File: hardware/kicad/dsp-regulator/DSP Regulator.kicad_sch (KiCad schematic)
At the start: 73 parts, among them J1 Conn_01x15_Socket, J2 Conn_01x15_Socket, J3 1935161, J4 Wire con, J5 Wire con, Q16 BSS138, Q2 BSS138, Q3 BSS138, U2 LM2596S-ADJ, U3 LM2596S-ADJ, U4 LM2596S-ADJ, U8 TS5A3157-DCKR

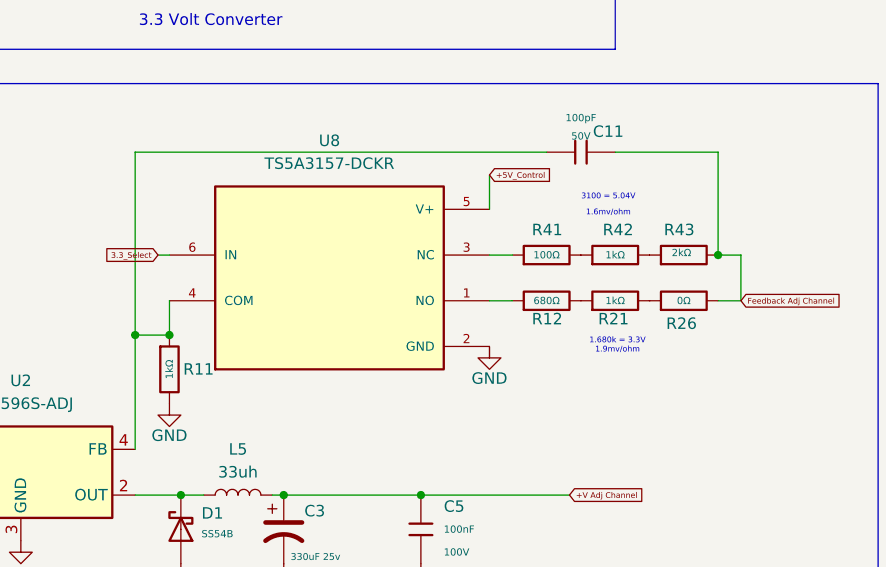
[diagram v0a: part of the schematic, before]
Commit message: hw(channel3): split J2 pin 06 to +V Adj Channel for CrowPanel 5V supply
- Split J2 pin 06 from +5V_Boot to dedicated +V Adj Channel net in
  both Rev-B schematics and netlists
- Reroute J21 pin 1 (CrowPanel display power) from +5V_Boot to
  +V Adj Channel in Rev-B HAT schematic and netlist
- PWR_FLAG at (123.19, 375.92) migrates to +V Adj Channel net via
  retained wire (374.65->375.92); J2 pins 08/10/12 remain on +5V_Boot
- DSP Regulator (PCB Rev-C prep): mark U8, R26, R43 as DNP;
  set R11=240 Ohm (lower FB->GND), R41=750 Ohm (future upper resistor)
- Update netlists manually to reflect schematic changes; re-export
  from KiCad GUI required for full ERC/DRC validation
- Connector contract: +V Adj Channel now PASS (was FAIL)

NOTE: R41 wire topology in DSP Regulator needs KiCad GUI edit to
connect as upper resistor (pin1->+V Adj Channel, pin2->FB).
VSENSE_ADJ+/-, ISET_MPU_Channel_3 failures are pre-existing.

Co-authored-by: Copilot <223556219+Copilot@users.noreply.github.com>
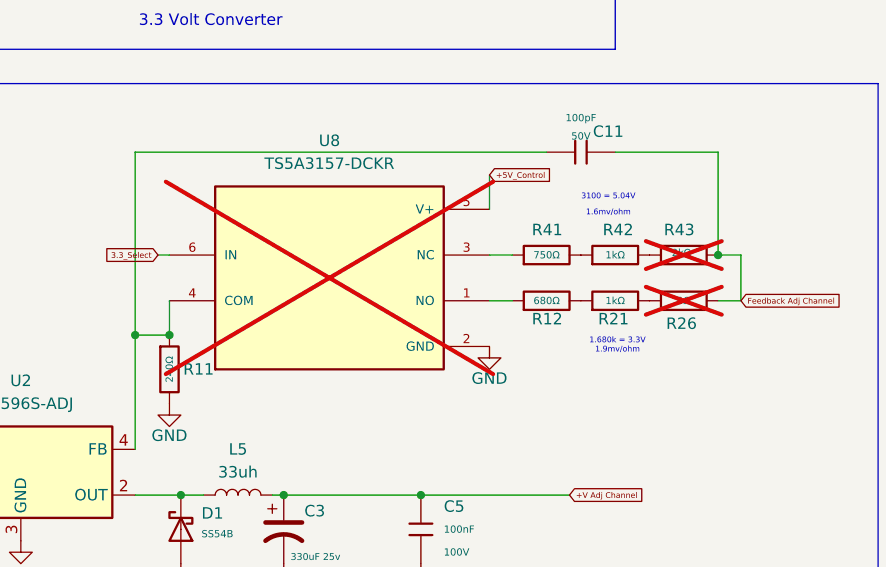
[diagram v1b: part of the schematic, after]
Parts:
- R11: value 1kΩ -> 240Ω
- R26, R43, U8: now not fitted
- R41: value 100Ω -> 750Ω
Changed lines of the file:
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@@
 		(in_bom yes)
 		(on_board yes)
-		(dnp no)
+		(dnp yes)
 		(property "Reference" "R26"
 			(at 239.776 189.23 90)
@@
 		(in_bom yes)
 		(on_board yes)
-		(dnp no)
+		(dnp yes)
 		(property "Reference" "R43"
 			(at 239.522 178.816 90)
@@
 			)
 		)
-		(property "Value" "1kΩ"
+		(property "Value" "240Ω"
 			(at 182.88 194.31 90)
 			(do_not_autoplace yes)
@@
 			)
 		)
-		(property "Value" "100Ω"
+		(property "Value" "750Ω"
 			(at 224.79 181.61 90)
 			(do_not_autoplace yes)
@@
 		(in_bom yes)
 		(on_board yes)
-		(dnp no)
+		(dnp yes)
 		(fields_autoplaced yes)
 		(property "Reference" "U8"
